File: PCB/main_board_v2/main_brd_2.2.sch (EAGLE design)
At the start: 53 parts, among them J2 SD-card Adapter, J3 E-paper Module, J4 Zigbee Module, J5 BATT, J6 CHARGER, J7 POGO_PINS, J8 ST-LINK, J9 additional I2C bus, U1 STM32F103C8T6-MODULE, U2 LF411CP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

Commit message: Created board 2.2
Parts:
- added C7: 100u, rcl:C-EU025-050X050
- added JP1: (no value), pinhead:PINHD-1X2
- added R16, R17: 10k, eagle-ltspice:RR0603
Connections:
- new net REED_MODE: JP1.1, R17.2, U1.PA_12
- new net WET_MODE: JP1.2, R16.2, U1.PA_11
- net GND: now also C7.2, R16.1, R17.1
- net LDO1_3.3V: now also C7.1
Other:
- moved on the sheet: J9, MS5803, TP3

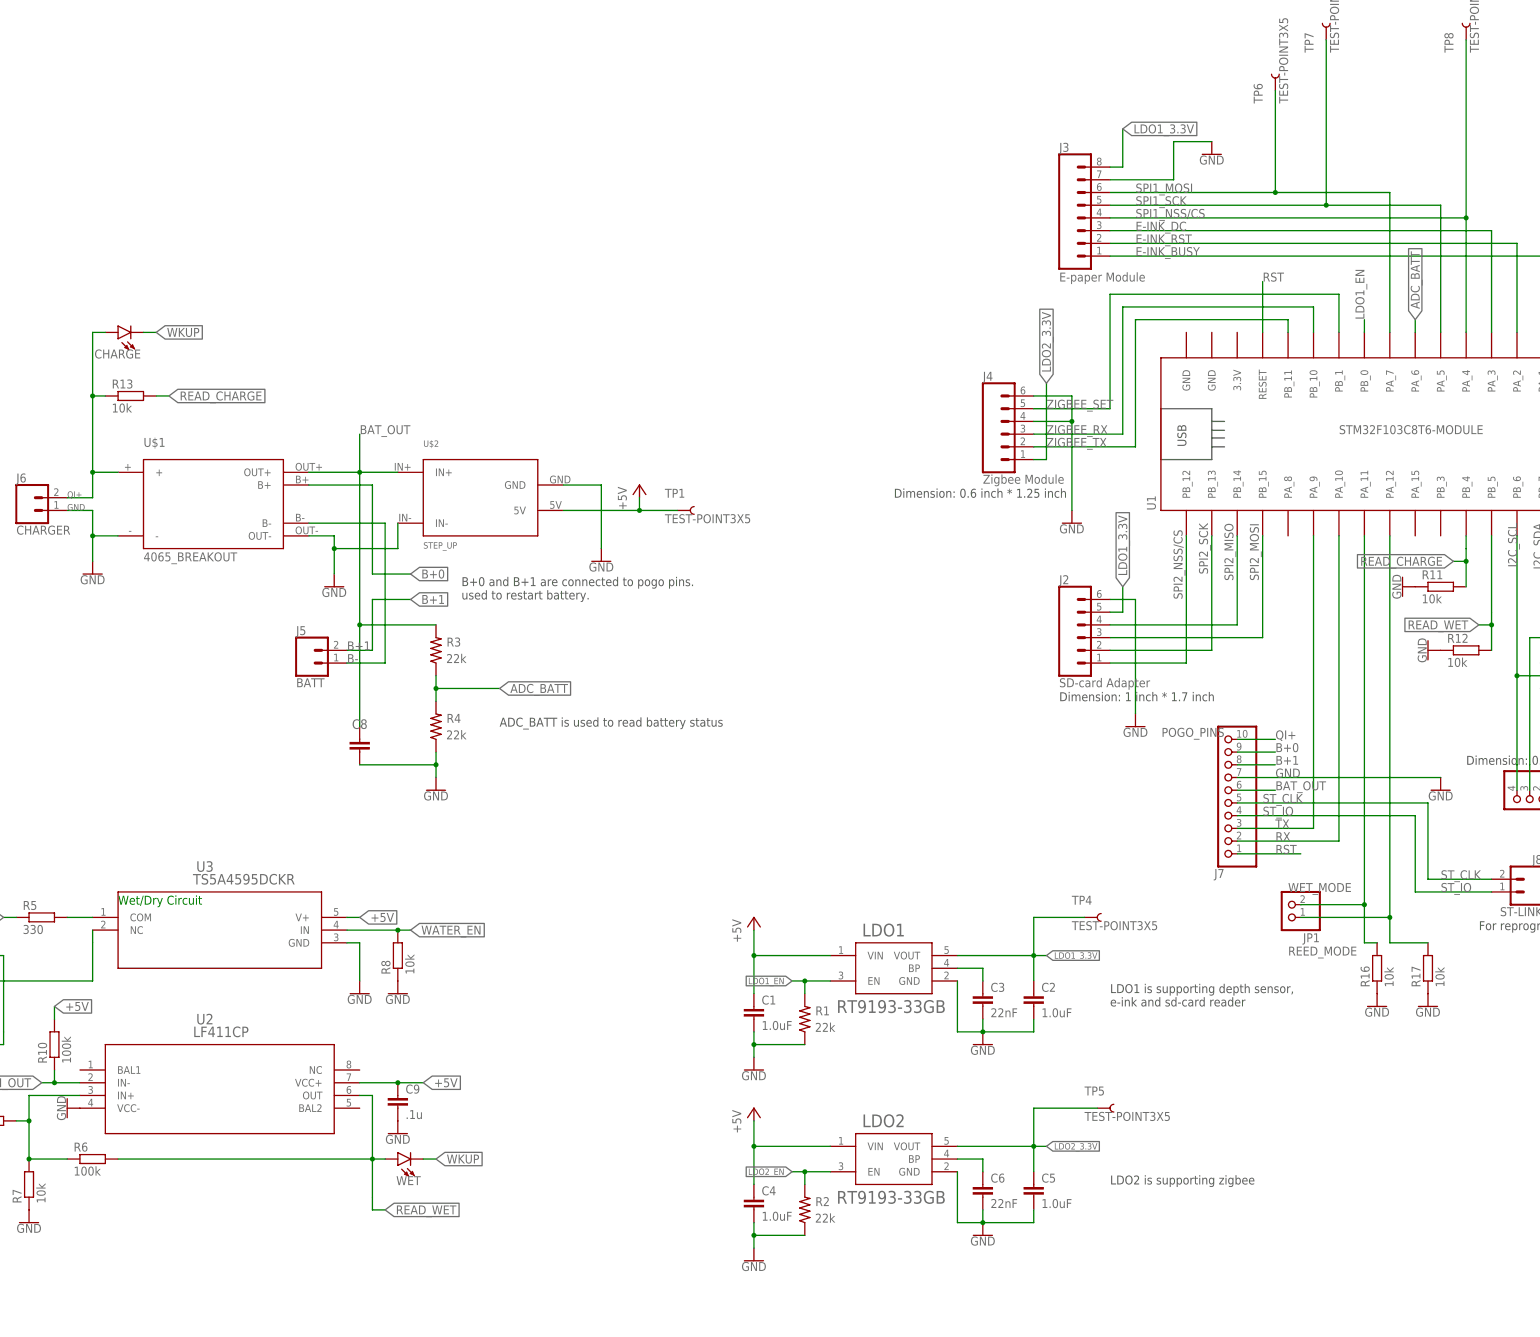
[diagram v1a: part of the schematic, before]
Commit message: Fixed wkup and routing
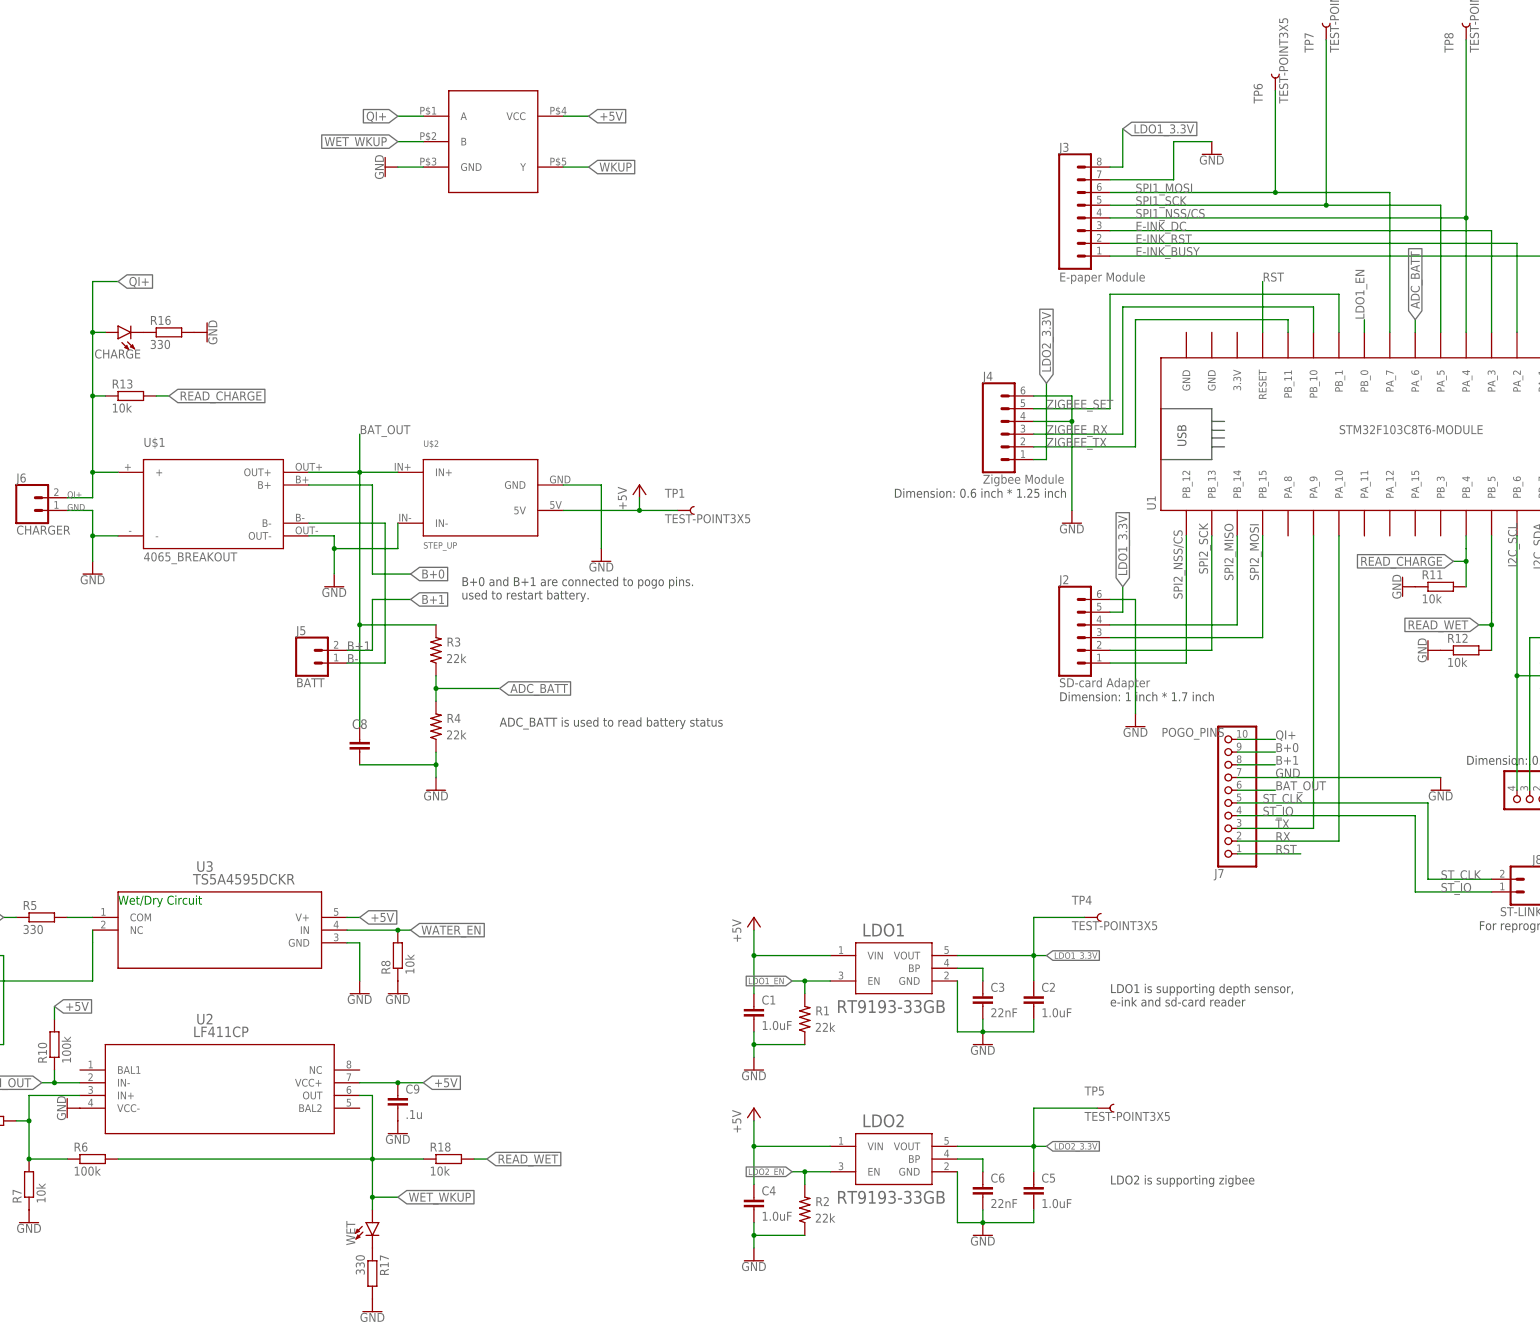
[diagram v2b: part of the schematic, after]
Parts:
- removed JP1: (no value), pinhead:PINHD-1X2
- added R18: 10k, eagle-ltspice:RR0603
- added U$3: 74LVC1G86SE-7, coral_power:74LVC1G86SE-7
- R16, R17: value 10k -> 330
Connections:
- removed net REED_MODE: JP1.1, R17.2, U1.PA_12
- removed net WET_MODE: JP1.2, R16.2, U1.PA_11
- new net N$10: R17.1, WET.C
- new net N$3: CHARGE.C, R16.1
- new net WET_WKUP: R18.1, R6.2, U$3.B, U2.OUT, WET.A
- net +5V: now also U$3.VCC
- net GND: now also R16.2, R17.2, U$3.GND; no longer R16.1, R17.1
- net QI+: now also U$3.A
- net READ_WET: now also R18.2; no longer R6.2, U2.OUT, WET.A
- net WKUP: now also U$3.Y; no longer CHARGE.C, WET.C
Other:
- moved on the sheet: R16, R17, WET
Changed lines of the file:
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@@
 <part name="SUPPLY1" library="SparkFun-PowerSymbols" deviceset="3.3V" device=""/>
 <part name="MS5803" library="pinhead" library_urn="urn:adsk.eagle:library:325" deviceset="PINHD-1X4" device="/90" package3d_urn="urn:adsk.eagle:package:22404/2"/>
-<part name="JP1" library="pinhead" library_urn="urn:adsk.eagle:library:325" deviceset="PINHD-1X2" device="" package3d_urn="urn:adsk.eagle:package:22435/2"/>
-<part name="R16" library="eagle-ltspice" library_urn="urn:adsk.eagle:library:217" deviceset="R" device="R0603" package3d_urn="urn:adsk.eagle:package:13302/1" value="10k"/>
-<part name="R17" library="eagle-ltspice" library_urn="urn:adsk.eagle:library:217" deviceset="R" device="R0603" package3d_urn="urn:adsk.eagle:package:13302/1" value="10k"/>
+<part name="C7" library="rcl" library_urn="urn:adsk.eagle:library:334" deviceset="C-EU" device="025-050X050" package3d_urn="urn:adsk.eagle:package:23633/1" value="100u"/>
+<part name="U$3" library="coral_power" deviceset="74LVC1G86SE-7" device=""/>
 <part name="GND25" library="SparkFun-PowerSymbols" deviceset="GND" device=""/>
+<part name="R16" library="eagle-ltspice" library_urn="urn:adsk.eagle:library:217" deviceset="R" device="R0603" package3d_urn="urn:adsk.eagle:package:13302/1" value="330"/>
+<part name="R17" library="eagle-ltspice" library_urn="urn:adsk.eagle:library:217" deviceset="R" device="R0603" package3d_urn="urn:adsk.eagle:package:13302/1" value="330"/>
 <part name="GND26" library="SparkFun-PowerSymbols" deviceset="GND" device=""/>
-<part name="C7" library="rcl" library_urn="urn:adsk.eagle:library:334" deviceset="C-EU" device="025-050X050" package3d_urn="urn:adsk.eagle:package:23633/1" value="100u"/>
+<part name="R18" library="eagle-ltspice" library_urn="urn:adsk.eagle:library:217" deviceset="R" device="R0603" package3d_urn="urn:adsk.eagle:package:13302/1" value="10k"/>
+<part name="GND27" library="SparkFun-PowerSymbols" deviceset="GND" device=""/>
 </parts>
 <sheets>
@@
 <instance part="GND19" gate="1" x="48.26" y="43.18" rot="R270"/>
 <instance part="CHARGE" gate="D1" x="58.42" y="198.12" rot="R90"/>
-<instance part="WET" gate="D1" x="114.3" y="33.02" rot="R90"/>
+<instance part="WET" gate="D1" x="109.22" y="20.32"/>
 <instance part="STATUS" gate="D1" x="378.46" y="200.66" rot="R90"/>
 <instance part="R11" gate="G$1" x="322.58" y="147.32"/>
@@
 <attribute name="VALUE" x="332.74" y="110.49" size="1.778" layer="96" rot="R270"/>
 </instance>
-<instance part="JP1" gate="G$1" x="292.1" y="83.82" rot="R180"/>
-<instance part="R16" gate="G$1" x="309.88" y="71.12" rot="R90"/>
-<instance part="R17" gate="G$1" x="320.04" y="71.12" rot="R90"/>
-<instance part="GND25" gate="1" x="320.04" y="63.5"/>
-<instance part="GND26" gate="1" x="309.88" y="63.5"/>
 <instance part="C7" gate="G$1" x="347.98" y="121.92" smashed="yes">
 <attribute name="NAME" x="348.9706" y="124.0028" size="1.905" layer="95" ratio="10" rot="SR0"/>
+</instance>
+<instance part="U$3" gate="G$1" x="134.62" y="236.22"/>
+<instance part="GND25" gate="1" x="111.76" y="231.14" smashed="yes" rot="R270">
+<attribute name="VALUE" x="111.506" y="231.14" size="1.778" layer="96" rot="R270" align="top-center"/>
+</instance>
+<instance part="R16" gate="G$1" x="68.58" y="198.12"/>
+<instance part="R17" gate="G$1" x="109.22" y="10.16" rot="R270"/>
+<instance part="GND26" gate="1" x="109.22" y="2.54"/>
+<instance part="R18" gate="G$1" x="124.46" y="33.02"/>
+<instance part="GND27" gate="1" x="76.2" y="198.12" smashed="yes" rot="R90">
+<attribute name="VALUE" x="76.454" y="198.12" size="1.778" layer="96" rot="R90" align="top-center"/>
 </instance>
 </instances>
@@
 </segment>
 <segment>
-<pinref part="R16" gate="G$1" pin="1"/>
+<pinref part="U$3" gate="G$1" pin="GND"/>
+<wire x1="119.38" y1="231.14" x2="114.3" y2="231.14" width="0.1524" layer="91"/>
+<pinref part="GND25" gate="1" pin="GND"/>
+</segment>
+<segment>
+<pinref part="R17" gate="G$1" pin="2"/>
 <pinref part="GND26" gate="1" pin="GND"/>
 </segment>
 <segment>
-<pinref part="R17" gate="G$1" pin="1"/>
-<pinref part="GND25" gate="1" pin="GND"/>
+<pinref part="R16" gate="G$1" pin="2"/>
+<pinref part="GND27" gate="1" pin="GND"/>
 </segment>
 </net>
@@
 <wire x1="53.34" y1="198.12" x2="55.88" y2="198.12" width="0.1524" layer="91"/>
 <junction x="53.34" y="185.42"/>
+<wire x1="53.34" y1="198.12" x2="53.34" y2="208.28" width="0.1524" layer="91"/>
+<wire x1="53.34" y1="208.28" x2="58.42" y2="208.28" width="0.1524" layer="91"/>
+<junction x="53.34" y="198.12"/>
+<label x="58.42" y="208.28" size="1.778" layer="95" xref="yes"/>
 </segment>
 <segment>
@@
 <wire x1="281.94" y1="116.84" x2="289.56" y2="116.84" width="0.1524" layer="91"/>
 <label x="289.56" y="116.84" size="1.778" layer="95"/>
+</segment>
+<segment>
+<pinref part="U$3" gate="G$1" pin="A"/>
+<wire x1="119.38" y1="241.3" x2="114.3" y2="241.3" width="0.1524" layer="91"/>
+<label x="114.3" y="241.3" size="1.778" layer="95" rot="R180" xref="yes"/>
 </segment>
 </net>
@@
 <wire x1="45.72" y1="60.96" x2="45.72" y2="63.5" width="0.1524" layer="91"/>
 <label x="45.72" y="63.5" size="1.778" layer="95" xref="yes"/>
+</segment>
+<segment>
+<pinref part="U$3" gate="G$1" pin="VCC"/>
+<wire x1="147.32" y1="241.3" x2="152.4" y2="241.3" width="0.1524" layer="91"/>
+<label x="152.4" y="241.3" size="1.778" layer="95" xref="yes"/>
 </segment>
 </net>
@@
 </segment>
 <segment>
-<pinref part="R6" gate="G$1" pin="2"/>
-<wire x1="58.42" y1="33.02" x2="109.22" y2="33.02" width="0.1524" layer="91"/>
-<wire x1="109.22" y1="33.02" x2="109.22" y2="45.72" width="0.1524" layer="91"/>
-<pinref part="U2" gate="A" pin="OUT"/>
-<wire x1="109.22" y1="45.72" x2="106.68" y2="45.72" width="0.1524" layer="91"/>
-<pinref part="WET" gate="D1" pin="A"/>
-<wire x1="109.22" y1="33.02" x2="111.76" y2="33.02" width="0.1524" layer="91"/>
-<junction x="109.22" y="33.02"/>
-<wire x1="109.22" y1="33.02" x2="109.22" y2="25.4" width="0.1524" layer="91"/>
-<wire x1="109.22" y1="25.4" x2="109.22" y2="22.86" width="0.1524" layer="91"/>
-<wire x1="109.22" y1="22.86" x2="111.76" y2="22.86" width="0.1524" layer="91"/>
-<label x="111.76" y="22.86" size="1.778" layer="95" xref="yes"/>
+<pinref part="R18" gate="G$1" pin="2"/>
+<wire x1="129.54" y1="33.02" x2="132.08" y2="33.02" width="0.1524" layer="91"/>
+<label x="132.08" y="33.02" size="1.778" layer="95" xref="yes"/>
 </segment>
 </net>
 <net name="WKUP" class="0">
-<segment>
-<pinref part="CHARGE" gate="D1" pin="C"/>
-<wire x1="63.5" y1="198.12" x2="66.04" y2="198.12" width="0.1524" layer="91"/>
-<label x="66.04" y="198.12" size="1.778" layer="95" xref="yes"/>
-</segment>
 <segment>
 <pinref part="U1" gate="G$1" pin="PA_0"/>
@@
 </segment>
 <segment>
-<pinref part="WET" gate="D1" pin="C"/>
-<wire x1="119.38" y1="33.02" x2="121.92" y2="33.02" width="0.1524" layer="91"/>
-<label x="121.92" y="33.02" size="1.778" layer="95" xref="yes"/>
+<pinref part="U$3" gate="G$1" pin="Y"/>
+<wire x1="147.32" y1="231.14" x2="152.4" y2="231.14" width="0.1524" layer="91"/>
+<label x="152.4" y="231.14" size="1.778" layer="95" xref="yes"/>
 </segment>
 </net>
@@
 </segment>
 </net>
-<net name="WET_MODE" class="0">
-<segment>
-<pinref part="U1" gate="G$1" pin="PA_11"/>
-<pinref part="JP1" gate="G$1" pin="2"/>
-<wire x1="307.34" y1="157.48" x2="307.34" y2="83.82" width="0.1524" layer="91"/>
-<wire x1="307.34" y1="83.82" x2="294.64" y2="83.82" width="0.1524" layer="91"/>
-<pinref part="R16" gate="G$1" pin="2"/>
-<wire x1="307.34" y1="83.82" x2="307.34" y2="76.2" width="0.1524" layer="91"/>
-<wire x1="307.34" y1="76.2" x2="309.88" y2="76.2" width="0.1524" layer="91"/>
-<junction x="307.34" y="83.82"/>
-<label x="292.1" y="86.36" size="1.778" layer="95"/>
-</segment>
-</net>
-<net name="REED_MODE" class="0">
-<segment>
-<pinref part="U1" gate="G$1" pin="PA_12"/>
-<pinref part="JP1" gate="G$1" pin="1"/>
-<wire x1="312.42" y1="157.48" x2="312.42" y2="81.28" width="0.1524" layer="91"/>
-<wire x1="312.42" y1="81.28" x2="294.64" y2="81.28" width="0.1524" layer="91"/>
-<pinref part="R17" gate="G$1" pin="2"/>
-<wire x1="312.42" y1="81.28" x2="312.42" y2="76.2" width="0.1524" layer="91"/>
-<wire x1="312.42" y1="76.2" x2="320.04" y2="76.2" width="0.1524" layer="91"/>
-<junction x="312.42" y="81.28"/>
-<label x="292.1" y="73.66" size="1.778" layer="95"/>
-</segment>
-</net>
+<net name="WET_WKUP" class="0">
+<segment>
+<pinref part="U$3" gate="G$1" pin="B"/>
+<wire x1="119.38" y1="236.22" x2="114.3" y2="236.22" width="0.1524" layer="91"/>
+<label x="114.3" y="236.22" size="1.778" layer="95" rot="R180" xref="yes"/>
+</segment>
+<segment>
+<pinref part="R6" gate="G$1" pin="2"/>
+<wire x1="58.42" y1="33.02" x2="109.22" y2="33.02" width="0.1524" layer="91"/>
+<wire x1="109.22" y1="33.02" x2="109.22" y2="45.72" width="0.1524" layer="91"/>
+<pinref part="U2" gate="A" pin="OUT"/>
+<wire x1="109.22" y1="45.72" x2="106.68" y2="45.72" width="0.1524" layer="91"/>
+<junction x="109.22" y="33.02"/>
+<pinref part="WET" gate="D1" pin="A"/>
+<wire x1="109.22" y1="22.86" x2="109.22" y2="25.4" width="0.1524" layer="91"/>
+<pinref part="R18" gate="G$1" pin="1"/>
+<wire x1="109.22" y1="25.4" x2="109.22" y2="33.02" width="0.1524" layer="91"/>
+<wire x1="119.38" y1="33.02" x2="109.22" y2="33.02" width="0.1524" layer="91"/>
+<wire x1="109.22" y1="25.4" x2="114.3" y2="25.4" width="0.1524" layer="91"/>
+<junction x="109.22" y="25.4"/>
+<label x="114.3" y="25.4" size="1.778" layer="95" xref="yes"/>
+</segment>
+</net>
+<net name="N$3" class="0">
+<segment>
+<pinref part="CHARGE" gate="D1" pin="C"/>
+<pinref part="R16" gate="G$1" pin="1"/>
+</segment>
+</net>
+<net name="N$10" class="0">
+<segment>
+<pinref part="WET" gate="D1" pin="C"/>
+<pinref part="R17" gate="G$1" pin="1"/>
+</segment>
+</net>
